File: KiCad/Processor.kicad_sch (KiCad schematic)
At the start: 19 parts, among them U16 Intel_P24T

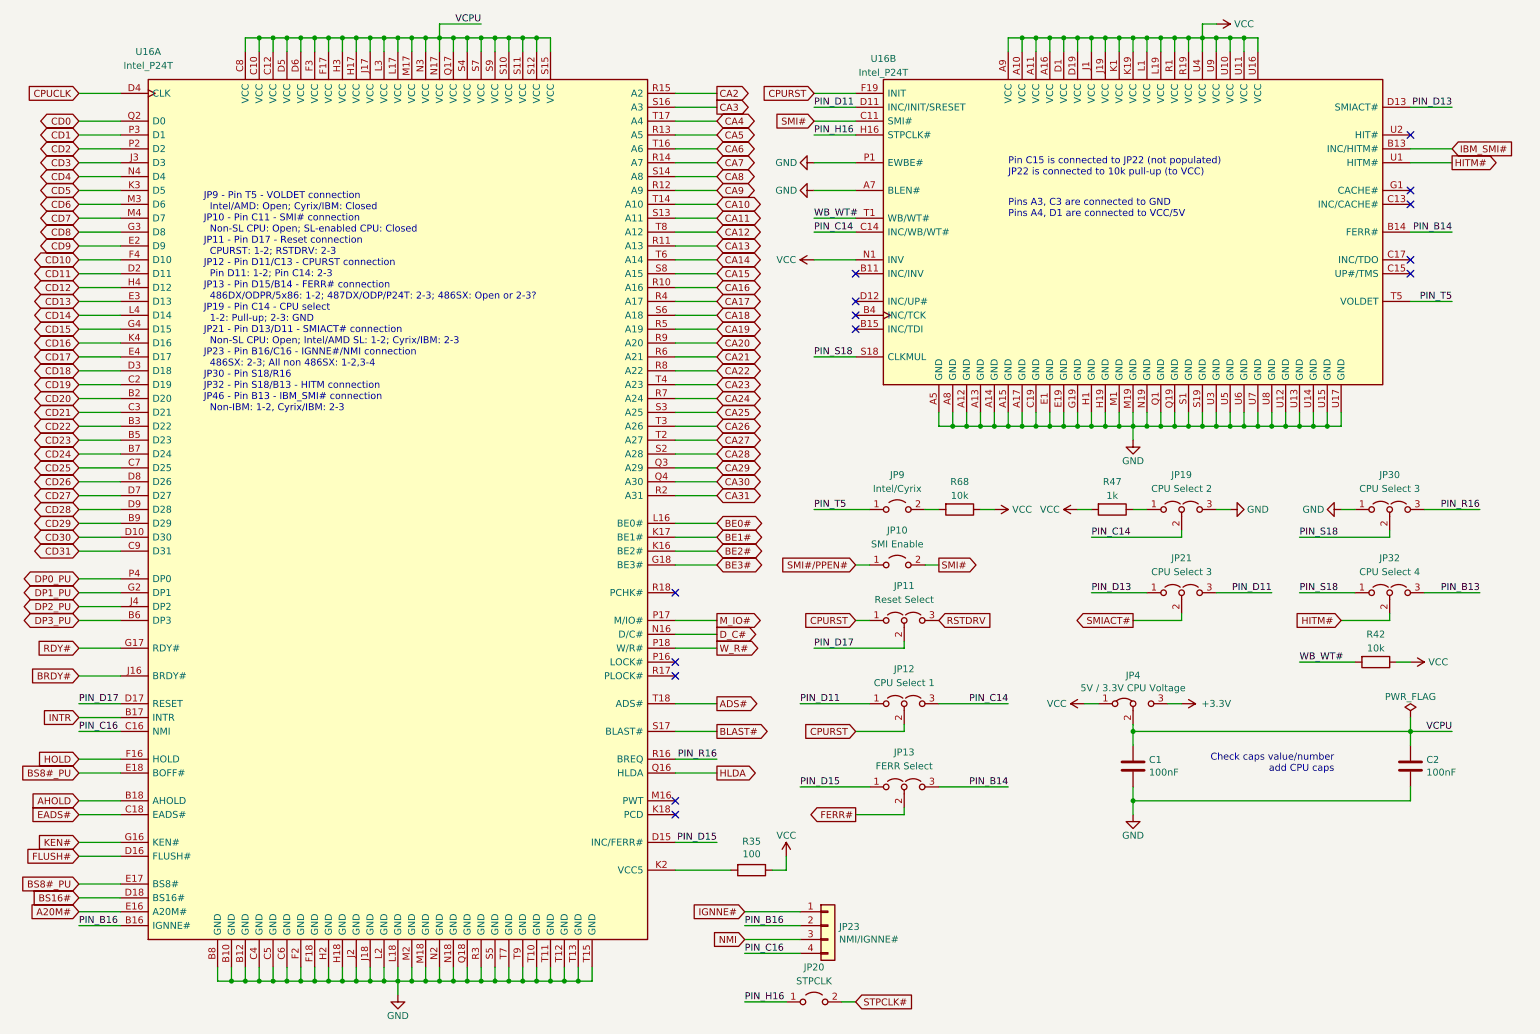
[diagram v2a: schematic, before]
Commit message: More schematic updates. Remove old KiCad files
Signed-off-by: Sergey Kiselev <skiselev@gmail.com>
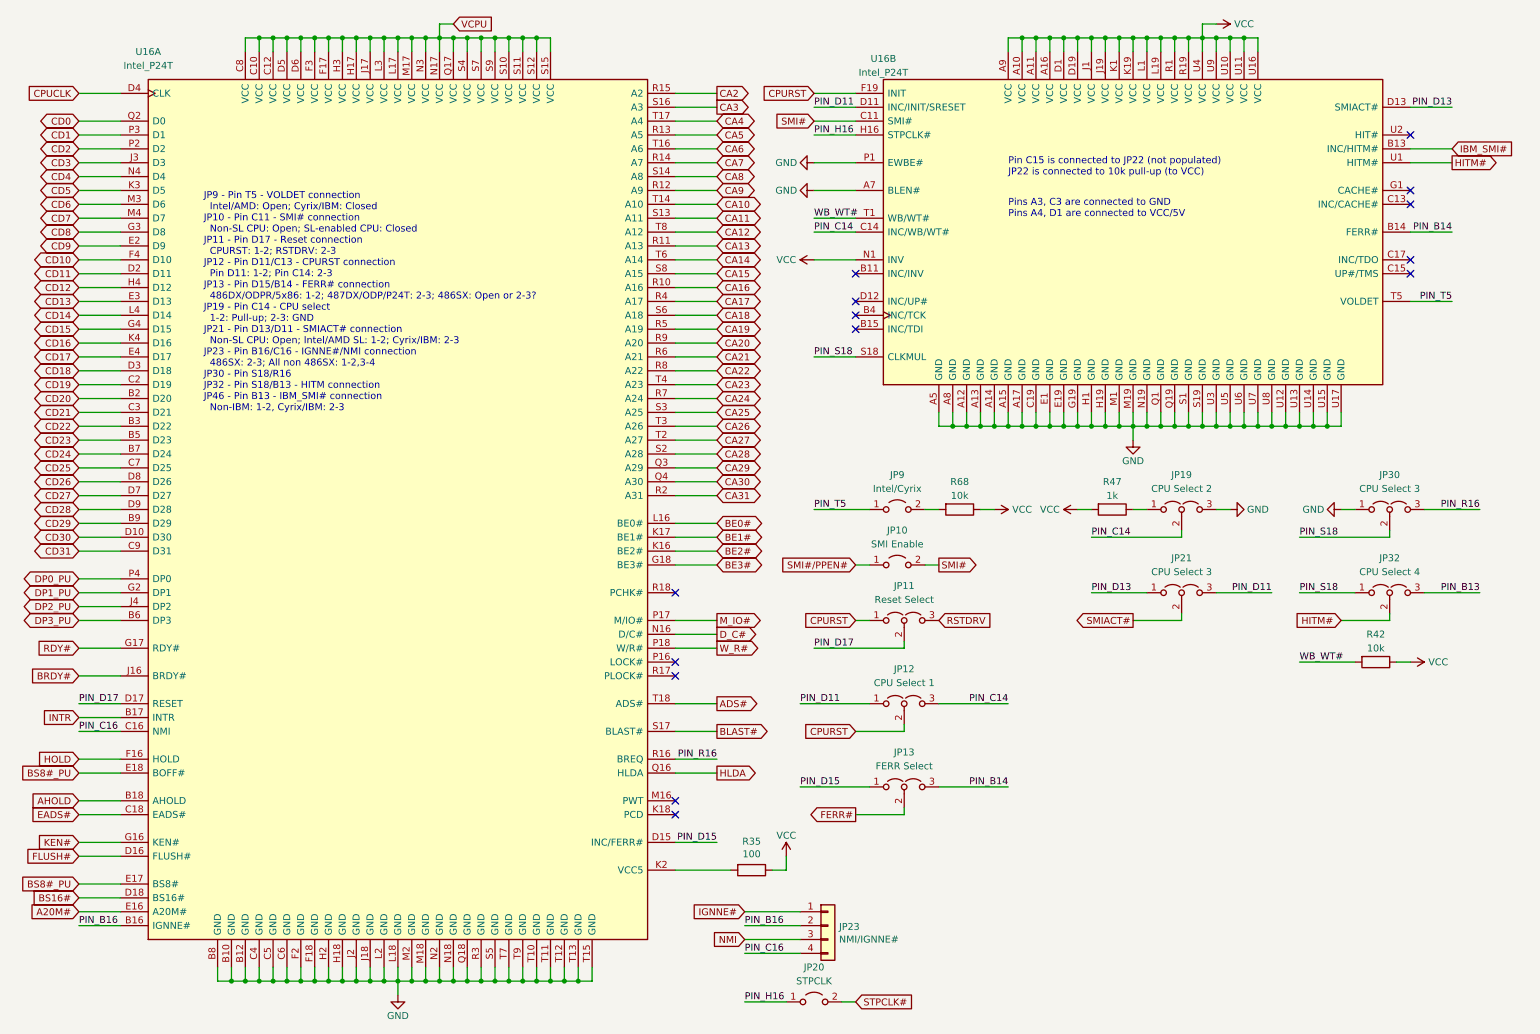
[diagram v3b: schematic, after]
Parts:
- removed C1, C2: 100nF, Capacitor_SMD:C_0603_1608Metric_Pad1.08x0.95mm_HandSolder, symbol Device:C
- removed JP4: 5V / 3.3V CPU Voltage, My_Components:Conn_Pin_Header_3x1_2.54mm, symbol Jumper:Jumper_3_Bridged12
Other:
- note removed: "Check caps value/number add CPU caps"
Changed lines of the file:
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@@
   (junction (at 203.2 88.9) (diameter 0) (color 0 0 0 0)
   )
-  (junction (at 215.9 144.78) (diameter 0) (color 0 0 0 0)
-  )
   (junction (at 203.2 17.78) (diameter 0) (color 0 0 0 0)
   )
@@
   (junction (at 218.44 17.78) (diameter 0) (color 0 0 0 0)
   )
-  (junction (at 266.7 144.78) (diameter 0) (color 0 0 0 0)
-  )
   (junction (at 220.98 17.78) (diameter 0) (color 0 0 0 0)
   )
@@
   )
   (junction (at 88.9 17.78) (diameter 0) (color 0 0 0 0)
-  )
-  (junction (at 215.9 157.48) (diameter 0) (color 0 0 0 0)
   )
   (junction (at 193.04 88.9) (diameter 0) (color 0 0 0 0)
@@
     (stroke (width 0) (type default) (color 0 0 0 0))
   )
-  (wire (pts (xy 215.9 147.32) (xy 215.9 144.78))
-    (stroke (width 0) (type default) (color 0 0 0 0))
-  )
   (wire (pts (xy 154.94 139.7) (xy 167.64 139.7))
     (stroke (width 0) (type default) (color 0 0 0 0))
@@
     (stroke (width 0) (type default) (color 0 0 0 0))
   )
-  (wire (pts (xy 222.25 139.7) (xy 224.79 139.7))
-    (stroke (width 0) (type default) (color 0 0 0 0))
-  )
   (wire (pts (xy 208.28 88.9) (xy 208.28 86.36))
     (stroke (width 0) (type default) (color 0 0 0 0))
@@
     (stroke (width 0) (type default) (color 0 0 0 0))
   )
-  (wire (pts (xy 215.9 143.51) (xy 215.9 144.78))
-    (stroke (width 0) (type default) (color 0 0 0 0))
-  )
   (wire (pts (xy 30.48 43.18) (xy 22.86 43.18))
     (stroke (width 0) (type default) (color 0 0 0 0))
   )
-  (wire (pts (xy 88.9 15.24) (xy 96.52 15.24))
+  (wire (pts (xy 88.9 15.24) (xy 91.44 15.24))
     (stroke (width 0) (type default) (color 0 0 0 0))
   )
@@
     (stroke (width 0) (type default) (color 0 0 0 0))
   )
-  (wire (pts (xy 266.7 142.24) (xy 266.7 144.78))
-    (stroke (width 0) (type default) (color 0 0 0 0))
-  )
   (wire (pts (xy 154.94 182.88) (xy 144.78 182.88))
     (stroke (width 0) (type default) (color 0 0 0 0))
@@
     (stroke (width 0) (type default) (color 0 0 0 0))
   )
-  (wire (pts (xy 215.9 157.48) (xy 266.7 157.48))
-    (stroke (width 0) (type default) (color 0 0 0 0))
-  )
   (wire (pts (xy 208.28 104.14) (xy 205.74 104.14))
     (stroke (width 0) (type default) (color 0 0 0 0))
@@
     (stroke (width 0) (type default) (color 0 0 0 0))
   )
-  (wire (pts (xy 266.7 144.78) (xy 266.7 147.32))
-    (stroke (width 0) (type default) (color 0 0 0 0))
-  )
   (wire (pts (xy 132.08 129.54) (xy 139.7 129.54))
     (stroke (width 0) (type default) (color 0 0 0 0))
@@
     (stroke (width 0) (type default) (color 0 0 0 0))
   )
-  (wire (pts (xy 266.7 154.94) (xy 266.7 157.48))
-    (stroke (width 0) (type default) (color 0 0 0 0))
-  )
   (wire (pts (xy 241.3 88.9) (xy 243.84 88.9))
     (stroke (width 0) (type default) (color 0 0 0 0))
@@
     (stroke (width 0) (type default) (color 0 0 0 0))
   )
-  (wire (pts (xy 215.9 154.94) (xy 215.9 157.48))
-    (stroke (width 0) (type default) (color 0 0 0 0))
-  )
   (wire (pts (xy 165.1 33.02) (xy 157.48 33.02))
     (stroke (width 0) (type default) (color 0 0 0 0))
@@
     (stroke (width 0) (type default) (color 0 0 0 0))
   )
-  (wire (pts (xy 266.7 144.78) (xy 274.32 144.78))
-    (stroke (width 0) (type default) (color 0 0 0 0))
-  )
   (wire (pts (xy 104.14 17.78) (xy 106.68 17.78))
     (stroke (width 0) (type default) (color 0 0 0 0))
   )
-  (wire (pts (xy 215.9 144.78) (xy 266.7 144.78))
-    (stroke (width 0) (type default) (color 0 0 0 0))
-  )
   (wire (pts (xy 208.28 119.38) (xy 218.44 119.38))
     (stroke (width 0) (type default) (color 0 0 0 0))
@@
     (stroke (width 0) (type default) (color 0 0 0 0))
   )
-  (wire (pts (xy 215.9 160.02) (xy 215.9 157.48))
-    (stroke (width 0) (type default) (color 0 0 0 0))
-  )
   (wire (pts (xy 73.66 190.5) (xy 76.2 190.5))
     (stroke (width 0) (type default) (color 0 0 0 0))
@@
     (stroke (width 0) (type default) (color 0 0 0 0))
   )
-  (wire (pts (xy 207.01 139.7) (xy 209.55 139.7))
-    (stroke (width 0) (type default) (color 0 0 0 0))
-  )
   (wire (pts (xy 109.22 190.5) (xy 111.76 190.5))
     (stroke (width 0) (type default) (color 0 0 0 0))
@@
   (wire (pts (xy 30.48 96.52) (xy 22.86 96.52))
     (stroke (width 0) (type default) (color 0 0 0 0))
-  )
-  (text "Check caps value/number\nadd CPU caps" (at 252.73 152.4 180)
-    (effects (font (size 1.27 1.27)) (justify right bottom))
   )
   (text "Pins A3, C3 are connected to GND\nPins A4, D1 are connected to VCC/5V\n"
@@
     (effects (font (size 1.27 1.27)) (justify right bottom))
   )
-  (label "VCPU" (at 96.52 15.24 180)
-    (effects (font (size 1.27 1.27)) (justify right bottom))
-  )
   (label "WB_WT#" (at 157.48 50.8 0)
     (effects (font (size 1.27 1.27)) (justify left bottom))
@@
     (effects (font (size 1.27 1.27)) (justify left bottom))
   )
-  (label "VCPU" (at 274.32 144.78 180)
-    (effects (font (size 1.27 1.27)) (justify right bottom))
-  )
   (global_label "CA12" (shape bidirectional) (at 139.7 53.34 0) (fields_autoplaced)
     (effects (font (size 1.27 1.27)) (justify left))
@@
     (effects (font (size 1.27 1.27)) (justify left))
     (property "Intersheet References" "${INTERSHEET_REFS}" (id 0) (at 146.8018 58.3406 0)
+      (effects (font (size 1.27 1.27)) (justify left) hide)
+    )
+  )
+  (global_label "VCPU" (shape input) (at 91.44 15.24 0) (fields_autoplaced)
+    (effects (font (size 1.27 1.27)) (justify left))
+    (property "Intersheet References" "${INTERSHEET_REFS}" (id 0) (at 98.7232 15.1606 0)
       (effects (font (size 1.27 1.27)) (justify left) hide)
     )
@@
     (pin "1")
   )
-  (symbol (lib_id "Jumper:Jumper_3_Bridged12") (at 215.9 139.7 0) (unit 1)
-    (in_bom yes) (on_board yes)
-    (property "Reference" "JP4" (id 0) (at 215.9 134.5184 0))
-    (property "Value" "5V / 3.3V CPU Voltage" (id 1) (at 215.9 136.8298 0))
-    (property "Footprint" "My_Components:Conn_Pin_Header_3x1_2.54mm" (id 2) (at 215.9 139.7 0)
-      (effects (font (size 1.27 1.27)) hide)
-    )
-    (property "Datasheet" "~" (id 3) (at 215.9 139.7 0)
-      (effects (font (size 1.27 1.27)) hide)
-    )
-    (pin "1")
-    (pin "2")
-    (pin "3")
-  )
-  (symbol (lib_id "power:VCC") (at 207.01 139.7 90) (unit 1)
-    (in_bom yes) (on_board yes)
-    (property "Reference" "#PWR0248" (id 0) (at 210.82 139.7 0)
-      (effects (font (size 1.27 1.27)) hide)
-    )
-    (property "Value" "VCC" (id 1) (at 201.93 139.7 90))
-    (property "Footprint" "" (id 2) (at 207.01 139.7 0)
-      (effects (font (size 1.27 1.27)) hide)
-    )
-    (property "Datasheet" "" (id 3) (at 207.01 139.7 0)
-      (effects (font (size 1.27 1.27)) hide)
-    )
-    (pin "1")
-  )
-  (symbol (lib_id "power:+3.3V") (at 224.79 139.7 270) (unit 1)
-    (in_bom yes) (on_board yes)
-    (property "Reference" "#PWR0249" (id 0) (at 220.98 139.7 0)
-      (effects (font (size 1.27 1.27)) hide)
-    )
-    (property "Value" "+3.3V" (id 1) (at 231.14 139.7 90))
-    (property "Footprint" "" (id 2) (at 224.79 139.7 0)
-      (effects (font (size 1.27 1.27)) hide)
-    )
-    (property "Datasheet" "" (id 3) (at 224.79 139.7 0)
-      (effects (font (size 1.27 1.27)) hide)
-    )
-    (pin "1")
-  )
-  (symbol (lib_id "Device:C") (at 215.9 151.13 0) (unit 1)
-    (in_bom yes) (on_board yes)
-    (property "Reference" "C1" (id 0) (at 218.821 149.9616 0)
-      (effects (font (size 1.27 1.27)) (justify left))
-    )
-    (property "Value" "100nF" (id 1) (at 218.821 152.273 0)
-      (effects (font (size 1.27 1.27)) (justify left))
-    )
-    (property "Footprint" "Capacitor_SMD:C_0603_1608Metric_Pad1.08x0.95mm_HandSolder" (id 2) (at 216.8652 154.94 0)
-      (effects (font (size 1.27 1.27)) hide)
-    )
-    (property "Datasheet" "~" (id 3) (at 215.9 151.13 0)
-      (effects (font (size 1.27 1.27)) hide)
-    )
-    (pin "1")
-    (pin "2")
-  )
-  (symbol (lib_id "power:GND") (at 215.9 160.02 0) (unit 1)
-    (in_bom yes) (on_board yes)
-    (property "Reference" "#PWR0252" (id 0) (at 215.9 166.37 0)
-      (effects (font (size 1.27 1.27)) hide)
-    )
-    (property "Value" "GND" (id 1) (at 215.9 163.83 0))
-    (property "Footprint" "" (id 2) (at 215.9 160.02 0)
-      (effects (font (size 1.27 1.27)) hide)
-    )
-    (property "Datasheet" "" (id 3) (at 215.9 160.02 0)
-      (effects (font (size 1.27 1.27)) hide)
-    )
-    (pin "1")
-  )
-  (symbol (lib_id "power:PWR_FLAG") (at 266.7 142.24 0) (unit 1)
-    (in_bom yes) (on_board yes)
-    (property "Reference" "#FLG0101" (id 0) (at 266.7 140.335 0)
-      (effects (font (size 1.27 1.27)) hide)
-    )
-    (property "Value" "PWR_FLAG" (id 1) (at 266.7 138.43 0))
-    (property "Footprint" "" (id 2) (at 266.7 142.24 0)
-      (effects (font (size 1.27 1.27)) hide)
-    )
-    (property "Datasheet" "~" (id 3) (at 266.7 142.24 0)
-      (effects (font (size 1.27 1.27)) hide)
-    )
-    (pin "1")
-  )
-  (symbol (lib_id "Device:C") (at 266.7 151.13 0) (unit 1)
-    (in_bom yes) (on_board yes)
-    (property "Reference" "C2" (id 0) (at 269.621 149.9616 0)
-      (effects (font (size 1.27 1.27)) (justify left))
-    )
-    (property "Value" "100nF" (id 1) (at 269.621 152.273 0)
-      (effects (font (size 1.27 1.27)) (justify left))
-    )
-    (property "Footprint" "Capacitor_SMD:C_0603_1608Metric_Pad1.08x0.95mm_HandSolder" (id 2) (at 267.6652 154.94 0)
-      (effects (font (size 1.27 1.27)) hide)
-    )
-    (property "Datasheet" "~" (id 3) (at 266.7 151.13 0)
-      (effects (font (size 1.27 1.27)) hide)
-    )
-    (pin "1")
-    (pin "2")
-  )
   (symbol (lib_id "Device:R") (at 146.05 170.18 270) (unit 1)
